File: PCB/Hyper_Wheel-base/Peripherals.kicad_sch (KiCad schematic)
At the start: 14 parts, among them U13 AS5600L-ASOM, U14 DRV5032FCDBZR, U3 AS5600L-ASOM, U8 DRV5032FCDBZR

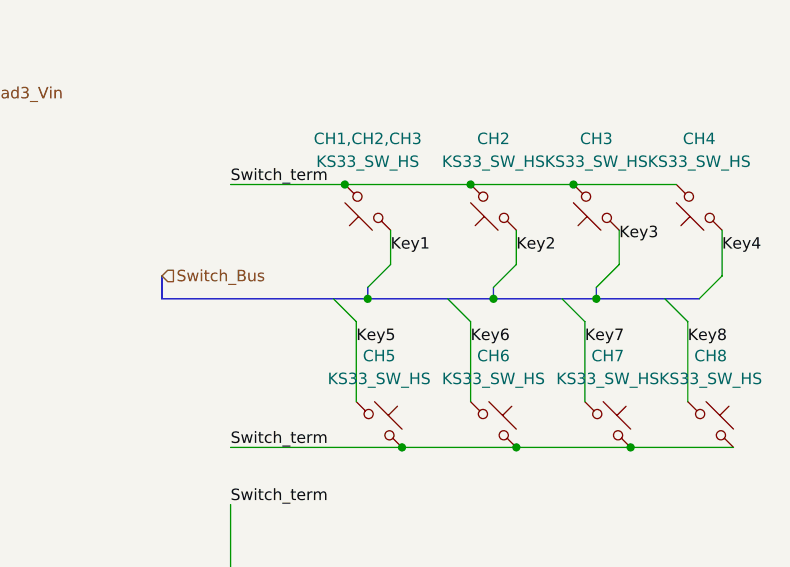
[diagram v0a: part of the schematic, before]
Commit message: Main board nearing RevA completion
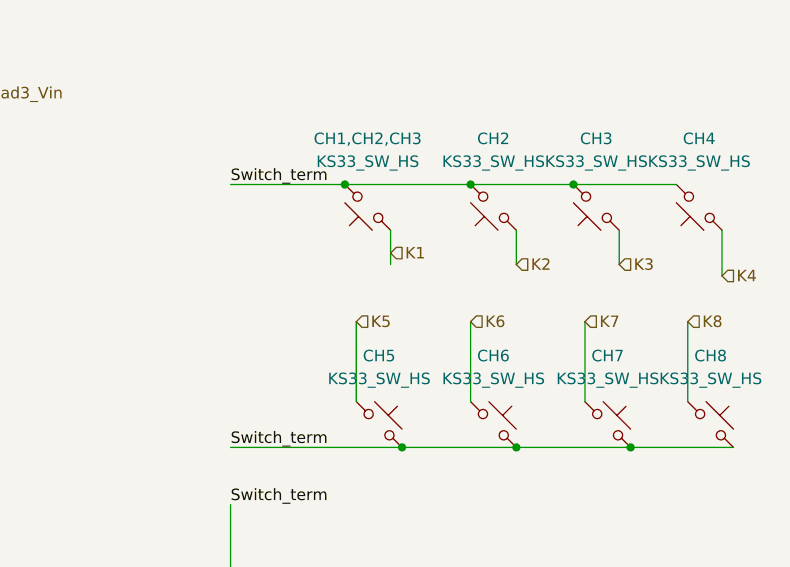
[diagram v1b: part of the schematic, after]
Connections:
- net Key1 renamed K1
- net Key2 renamed K2
- net Key3 renamed K3
- net Key4 renamed K4
- net Key5 renamed K5
- net Key6 renamed K6
- net Key7 renamed K7
- net Key8 renamed K8
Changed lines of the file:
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@@
-	)
-	(junction
-		(at 234.95 67.31)
-		(diameter 0)
-		(color 0 0 0 0)
 	)
 	(junction
@@
 	)
 	(junction
-		(at 246.38 67.31)
-		(diameter 0)
-		(color 0 0 0 0)
-	)
-	(junction
-		(at 220.98 67.31)
-		(diameter 0)
-		(color 0 0 0 0)
-	)
-	(junction
 		(at 69.85 118.11)
 		(diameter 0)
@@
 		(color 0 0 0 0)
 	)
-	(bus_entry
-		(at 254 67.31)
-		(size 2.54 2.54)
-		(stroke
-			(width 0)
-			(type default)
-		)
-	)
-	(bus_entry
-		(at 220.98 66.04)
-		(size 2.54 -2.54)
-		(stroke
-			(width 0)
-			(type default)
-		)
-	)
-	(bus_entry
-		(at 234.95 66.04)
-		(size 2.54 -2.54)
-		(stroke
-			(width 0)
-			(type default)
-		)
-	)
-	(bus_entry
-		(at 217.17 67.31)
-		(size 2.54 2.54)
-		(stroke
-			(width 0)
-			(type default)
-		)
-	)
-	(bus_entry
-		(at 257.81 67.31)
-		(size 2.54 -2.54)
-		(stroke
-			(width 0)
-			(type default)
-		)
-	)
-	(bus_entry
-		(at 242.57 67.31)
-		(size 2.54 2.54)
-		(stroke
-			(width 0)
-			(type default)
-		)
-	)
-	(bus_entry
-		(at 246.38 66.04)
-		(size 2.54 -2.54)
-		(stroke
-			(width 0)
-			(type default)
-		)
-	)
-	(bus_entry
-		(at 229.87 67.31)
-		(size 2.54 2.54)
-		(stroke
-			(width 0)
-			(type default)
-		)
-	)
 	(wire
 		(pts
@@
 	(wire
 		(pts
+			(xy 260.35 59.69) (xy 260.35 64.77)
+		)
+		(stroke
+			(width 0)
+			(type default)
+		)
+	)
+	(wire
+		(pts
 			(xy 250.19 83.82) (xy 261.62 83.82)
 		)
@@
 		)
 	)
-	(bus
-		(pts
-			(xy 234.95 67.31) (xy 246.38 67.31)
-		)
-		(stroke
-			(width 0)
-			(type default)
-		)
-	)
 	(wire
 		(pts
@@
 		)
 	)
-	(bus
-		(pts
-			(xy 246.38 66.04) (xy 246.38 67.31)
-		)
-		(stroke
-			(width 0)
-			(type default)
-		)
-	)
 	(wire
 		(pts
@@
 	(wire
 		(pts
-			(xy 260.35 64.77) (xy 260.35 59.69)
-		)
-		(stroke
-			(width 0)
-			(type default)
-		)
-	)
-	(wire
-		(pts
 			(xy 60.96 113.03) (xy 80.01 113.03)
 		)
@@
 		)
 	)
-	(bus
-		(pts
-			(xy 220.98 67.31) (xy 234.95 67.31)
-		)
-		(stroke
-			(width 0)
-			(type default)
-		)
-	)
-	(bus
-		(pts
-			(xy 234.95 66.04) (xy 234.95 67.31)
-		)
-		(stroke
-			(width 0)
-			(type default)
-		)
-	)
 	(wire
 		(pts
@@
 		)
 	)
-	(bus
-		(pts
-			(xy 246.38 67.31) (xy 257.81 67.31)
-		)
-		(stroke
-			(width 0)
-			(type default)
-		)
-	)
 	(wire
 		(pts
@@
 		)
 	)
-	(bus
-		(pts
-			(xy 198.12 67.31) (xy 198.12 64.77)
-		)
-		(stroke
-			(width 0)
-			(type default)
-		)
-	)
 	(wire
 		(pts
@@
 		)
 	)
-	(bus
-		(pts
-			(xy 198.12 67.31) (xy 220.98 67.31)
-		)
-		(stroke
-			(width 0)
-			(type default)
-		)
-	)
 	(wire
 		(pts
@@
 		(pts
 			(xy 43.18 73.66) (xy 59.69 73.66)
-		)
-		(stroke
-			(width 0)
-			(type default)
-		)
-	)
-	(bus
-		(pts
-			(xy 220.98 66.04) (xy 220.98 67.31)
 		)
 		(stroke
@@
 		)
 	)
-	(label "Key1"
-		(at 223.52 62.23 0)
-		(effects
-			(font
-				(size 1.27 1.27)
-			)
-			(justify left bottom)
-		)
-	)
 	(label "SCL2"
 		(at 110.49 73.66 0)
@@
 		)
 	)
-	(label "Key7"
-		(at 245.11 72.39 0)
-		(effects
-			(font
-				(size 1.27 1.27)
-			)
-			(justify left bottom)
-		)
-	)
 	(label "SCL1"
 		(at 82.55 115.57 0)
@@
 		)
 	)
-	(label "Key6"
-		(at 232.41 72.39 0)
-		(effects
-			(font
-				(size 1.27 1.27)
-			)
-			(justify left bottom)
-		)
-	)
 	(label "SDA1"
 		(at 110.49 44.45 0)
@@
 		)
 	)
-	(label "Key2"
-		(at 237.49 62.23 0)
-		(effects
-			(font
-				(size 1.27 1.27)
-			)
-			(justify left bottom)
-		)
-	)
 	(label "Switch_term"
 		(at 205.74 83.82 0)
@@
 		)
 	)
-	(label "Key4"
-		(at 260.35 62.23 0)
-		(effects
-			(font
-				(size 1.27 1.27)
-			)
-			(justify left bottom)
-		)
-	)
-	(label "Key3"
-		(at 248.92 60.96 0)
-		(effects
-			(font
-				(size 1.27 1.27)
-			)
-			(justify left bottom)
-		)
-	)
-	(label "Key5"
-		(at 219.71 72.39 0)
-		(effects
-			(font
-				(size 1.27 1.27)
-			)
-			(justify left bottom)
-		)
-	)
 	(label "SCL2"
 		(at 172.72 33.02 0)
-		(effects
-			(font
-				(size 1.27 1.27)
-			)
-			(justify left bottom)
-		)
-	)
-	(label "Key8"
-		(at 256.54 72.39 0)
 		(effects
 			(font
@@
 		)
 	)
+	(hierarchical_label "K5"
+		(shape input)
+		(at 219.71 69.85 0)
+		(effects
+			(font
+				(size 1.27 1.27)
+			)
+			(justify left)
+		)
+	)
+	(hierarchical_label "K3"
+		(shape input)
+		(at 248.92 63.5 0)
+		(effects
+			(font
+				(size 1.27 1.27)
+			)
+			(justify left)
+		)
+	)
 	(hierarchical_label "Hall_1"
 		(shape input)
@@
 		)
 	)
+	(hierarchical_label "K4"
+		(shape input)
+		(at 260.35 64.77 0)
+		(effects
+			(font
+				(size 1.27 1.27)
+			)
+			(justify left)
+		)
+	)
 	(hierarchical_label "Load3_Vin"
 		(shape input)
@@
 		)
 	)
+	(hierarchical_label "K1"
+		(shape input)
+		(at 223.52 62.23 0)
+		(effects
+			(font
+				(size 1.27 1.27)
+			)
+			(justify left)
+		)
+	)
+	(hierarchical_label "K8"
+		(shape input)
+		(at 256.54 69.85 0)
+		(effects
+			(font
+				(size 1.27 1.27)
+			)
+			(justify left)
+		)
+	)
 	(hierarchical_label "SCL-2"
 		(shape input)
@@
 		)
 	)
-	(hierarchical_label "Switch_Bus"
-		(shape input)
-		(at 198.12 64.77 0)
+	(hierarchical_label "K6"
+		(shape input)
+		(at 232.41 69.85 0)
+		(effects
+			(font
+				(size 1.27 1.27)
+			)
+			(justify left)
+		)
+	)
+	(hierarchical_label "K7"
+		(shape input)
+		(at 245.11 69.85 0)
 		(effects
 			(font
@@
 		(effects
 			(font
+				(size 1.27 1.27)
+			)
+			(justify left)
+		)
+	)
+	(hierarchical_label "K2"
+		(shape input)
+		(at 237.49 63.5 0)
+		(effects
+			(font

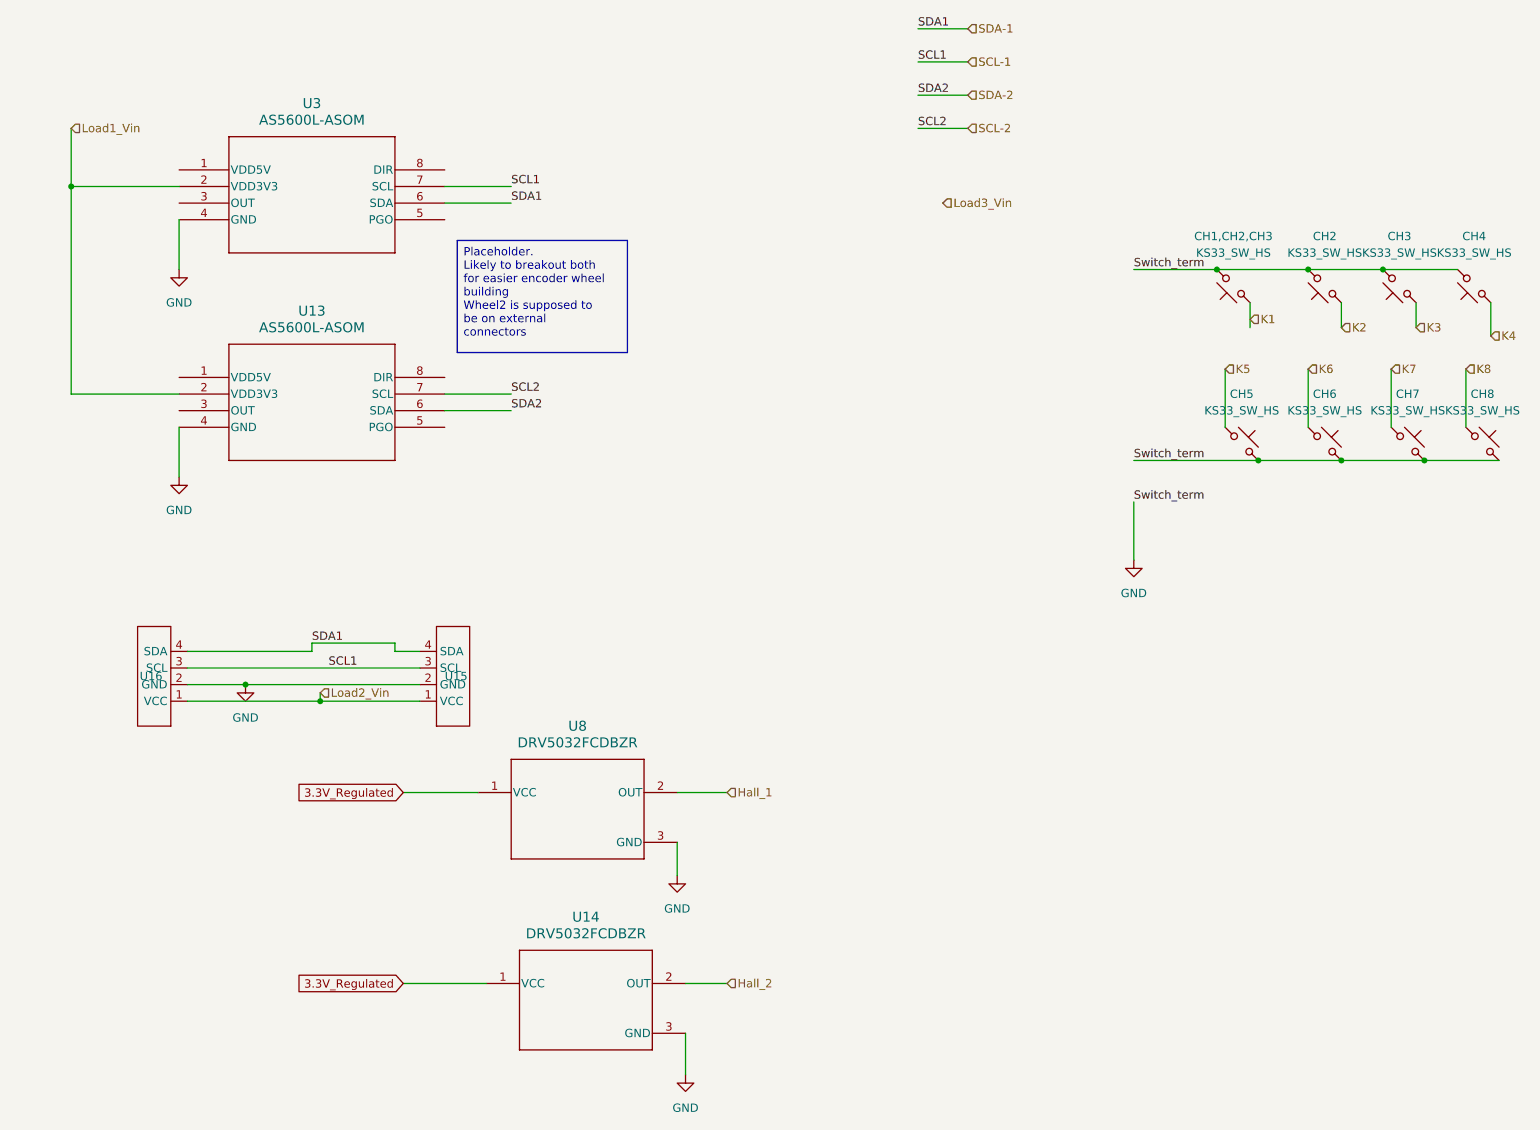
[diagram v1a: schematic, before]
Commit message: power plane added,  passes Peer review
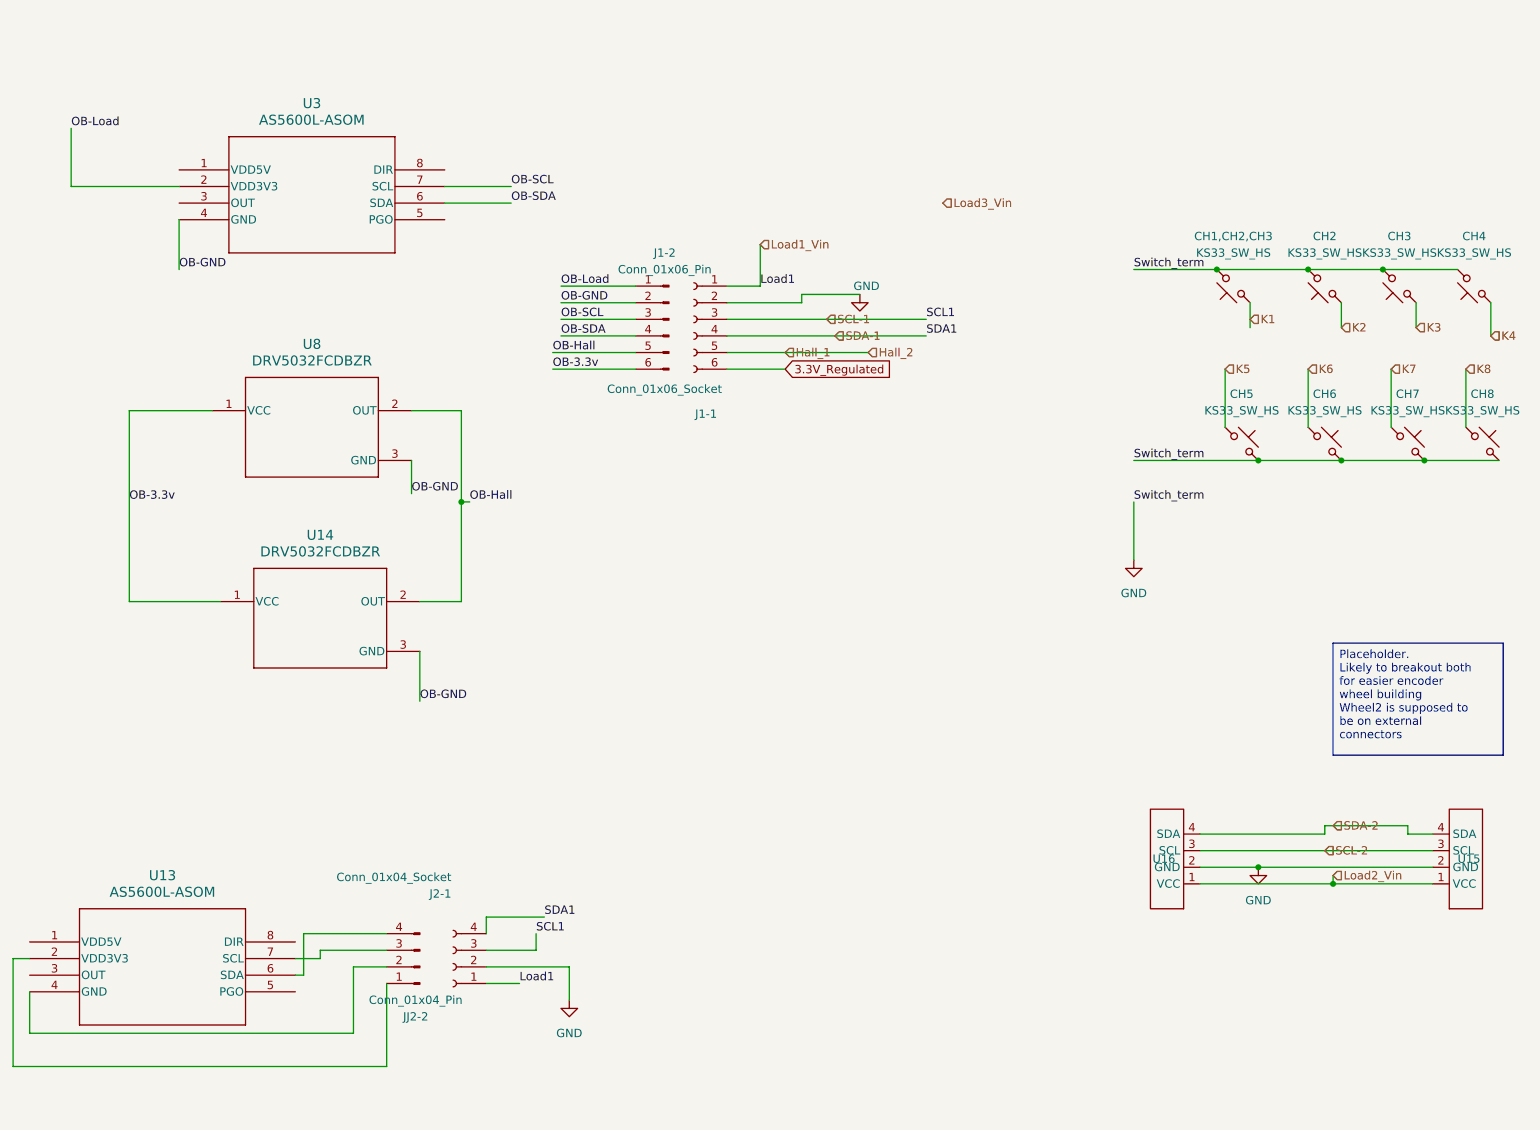
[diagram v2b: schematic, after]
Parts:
- added J1-1: Conn_01x06_Socket, Connector_PinHeader_2.54mm:PinHeader_1x06_P2.54mm_Vertical, symbol Connector:Conn_01x06_Socket
- added J1-2: Conn_01x06_Pin, symbol Connector:Conn_01x06_Pin
- added J2-1: Conn_01x04_Socket, Connector_PinHeader_2.54mm:PinHeader_1x04_P2.54mm_Vertical, symbol Connector:Conn_01x04_Socket
- added JJ2-2: Conn_01x04_Pin, symbol Connector:Conn_01x04_Pin
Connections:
- net 3.3V_Regulated: now also J1-1.6 (Pin_6); no longer U14.1 (VCC), U8.1 (VCC)
- net GND: now also J1-1.2 (Pin_2), J2-1.2 (Pin_2); no longer U13.4 (GND), U14.3 (GND), U3.4 (GND), U8.3 (GND)
- net Hall_1: now also J1-1.5 (Pin_5); no longer U8.2 (OUT)
- net Load1_Vin: now also J1-1.1 (Pin_1), J2-1.1 (Pin_1); no longer U13.2 (VDD3V3), U3.2 (VDD3V3)
- net SCL-1: now also J1-1.3 (Pin_3), J2-1.3 (Pin_3); no longer U15.3 (SCL), U16.3 (SCL), U3.7 (SCL)
- net SCL-2: now also U15.3 (SCL), U16.3 (SCL); no longer U13.7 (SCL)
- net SDA-1: now also J1-1.4 (Pin_4), J2-1.4 (Pin_4); no longer U15.4 (SDA), U16.4 (SDA), U3.6 (SDA)
- net SDA-2: now also U15.4 (SDA), U16.4 (SDA); no longer U13.6 (SDA)
- net Hall_2 renamed OB-Hall
- net OB-Hall: now also U8.2 (OUT), J1-2.5 (Pin_5)
- new net: JJ2-2.1 (Pin_1), U13.2 (VDD3V3)
- new net: JJ2-2.2 (Pin_2), U13.4 (GND)
- new net: JJ2-2.4 (Pin_4), U13.6 (SDA)
- new net: JJ2-2.3 (Pin_3), U13.7 (SCL)
- new net OB-3.3v: J1-2.6 (Pin_6), U14.1 (VCC), U8.1 (VCC)
- new net OB-GND: J1-2.2 (Pin_2), U14.3 (GND), U3.4 (GND), U8.3 (GND)
- new net OB-Load: J1-2.1 (Pin_1), U3.2 (VDD3V3)
- new net OB-SCL: J1-2.3 (Pin_3), U3.7 (SCL)
- new net OB-SDA: J1-2.4 (Pin_4), U3.6 (SDA)
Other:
- moved on the sheet: U13, U14, U15, U16, U8

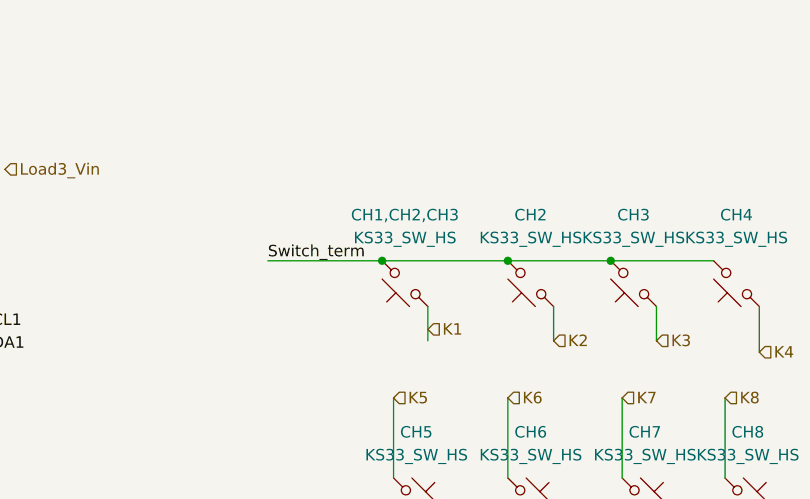
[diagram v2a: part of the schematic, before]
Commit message: XIAO based test board complete
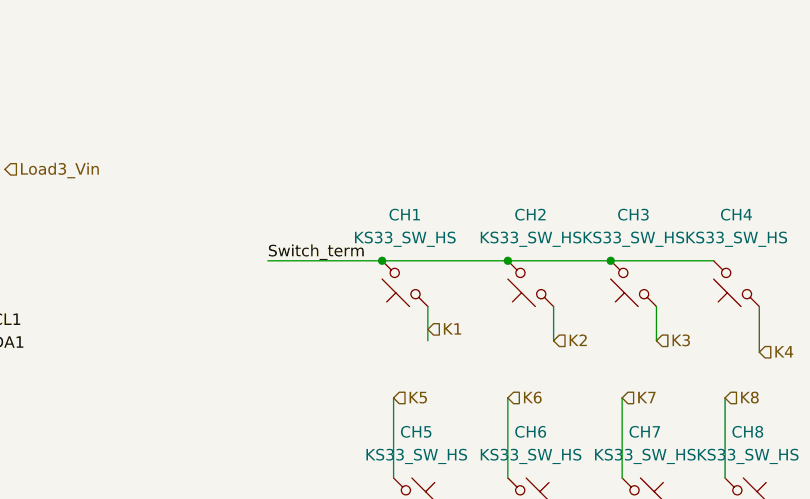
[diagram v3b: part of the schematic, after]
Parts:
- J1-1, J2-1: KiLib_Generator (none) -> connector/pin_header_socket
- renumbered CH1,CH2,CH3 to CH1
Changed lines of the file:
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@@
+			)
+		)
+		(property "KiLib_Generator" "connector/pin_header_socket"
+			(at 101.6 161.29 0)
+			(hide yes)
+			(show_name no)
+			(do_not_autoplace no)
+			(effects
+				(font
+					(size 1.27 1.27)
+				)
 			)
 		)
@@
 		(dnp no)
 		(fields_autoplaced yes)
-		(property "Reference" "CH1,CH2,CH3"
+		(property "Reference" "CH1"
 			(at 220.98 49.53 0)
 			(show_name no)
@@
 			(project "Hyper_Wheel-base"
 				(path "/3f05eeb1-03f9-49d1-8a58-0bc3d5427d25/27e14a4a-7907-4947-a1bd-66ab05fca5b6"
-					(reference "CH1,CH2,CH3")
+					(reference "CH1")
 					(unit 1)
 				)
@@
 			(at 138.43 62.23 0)
 			(hide yes)
+			(show_name no)
+			(do_not_autoplace no)
+			(effects
+				(font
+					(size 1.27 1.27)
+				)
+			)
+		)
+		(property "KiLib_Generator" "connector/pin_header_socket"
+			(at 138.43 62.23 0)
+			(hide yes)

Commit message: Rev B Xiao.  migrated changes to main
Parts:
- added JP3, JP4: Jumper_3_Bridged12, Jumper:SolderJumper-3_P1.3mm_Bridged12_Pad1.0x1.5mm, symbol Jumper:Jumper_3_Bridged12
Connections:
- net GND: now also JP3.2 (C); no longer U15.2 (GND), U16.2 (GND)
- net Load2_Vin: now also JP4.2 (C); no longer U15.1 (VCC), U16.1 (VCC)
- new net: JP3.1 (A), JP4.3 (B), U15.1 (VCC), U16.1 (VCC)
- new net: JP3.3 (B), JP4.1 (A), U15.2 (GND), U16.2 (GND)
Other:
- moved on the sheet: U16
